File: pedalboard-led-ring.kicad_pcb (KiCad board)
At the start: 2 copper layers, 28 x 28 mm, 26 parts, among them J1 Conn_02x02_Odd_Even

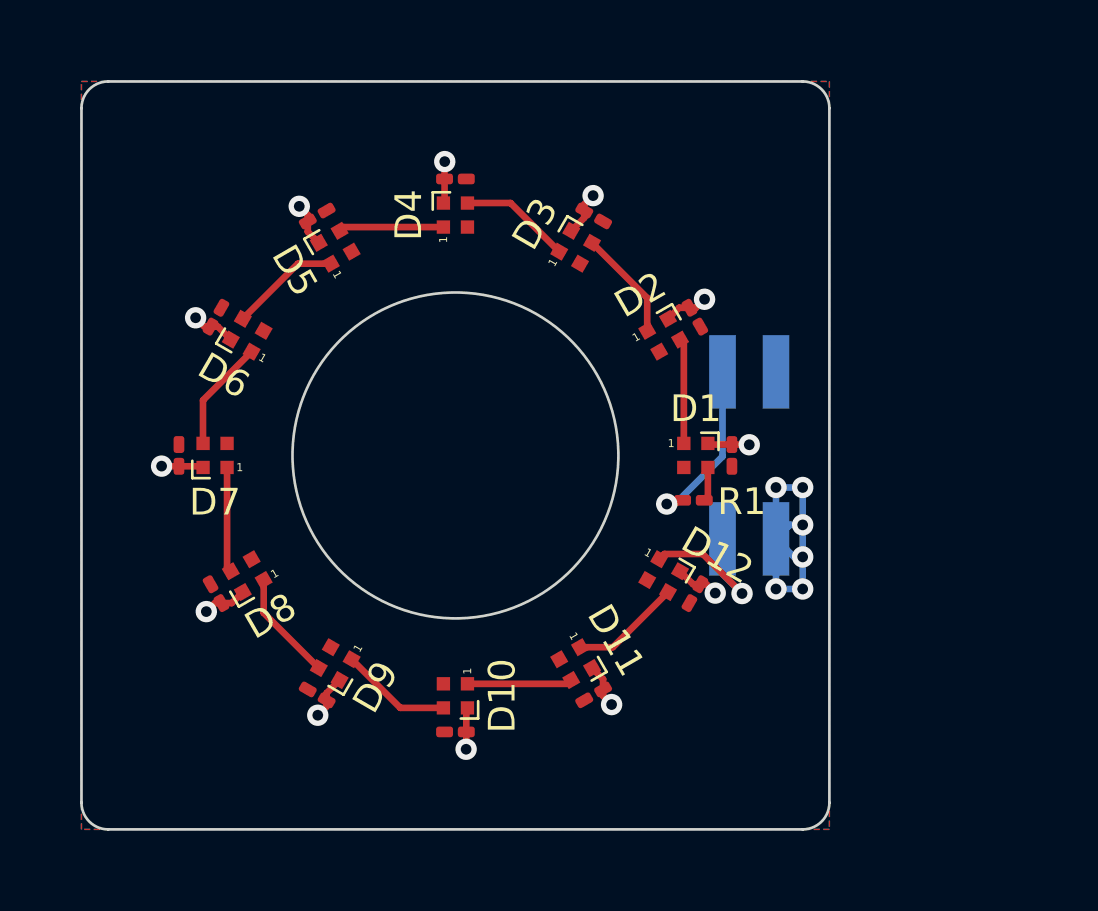
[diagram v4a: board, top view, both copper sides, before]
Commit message: Add 2nd connector port
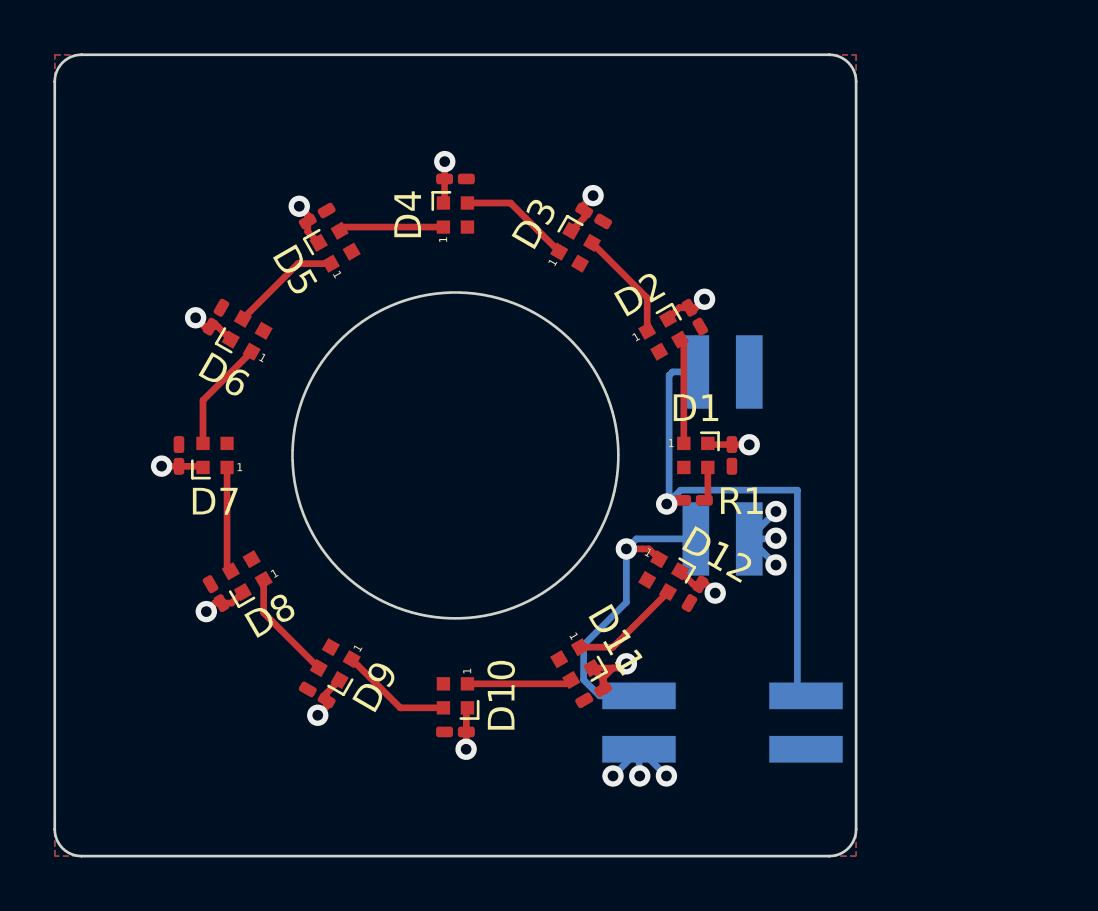
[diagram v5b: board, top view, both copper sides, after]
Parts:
- added J2: edge, Connector_PinSocket_2.00mm:PinSocket_2x02_P2.00mm_Vertical_SMD, B.Cu at (90.0, 70.0)
- J1: value Conn_02x02_Odd_Even -> middle
- moved J1 1.00 mm to (90.0, 60.0)
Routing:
- net Net-(J1-Pin_3): track 6.50 -> 19.4 mm
- net Net-(D12-DOUT): track 6.18 -> 12.0 mm
- net GND: track 12.1 -> 7.71 mm
- net VCC: track 19.3 -> 21.0 mm
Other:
- board size 28 x 28 mm -> 30 x 30 mm

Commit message: Move vias outside of keep out area
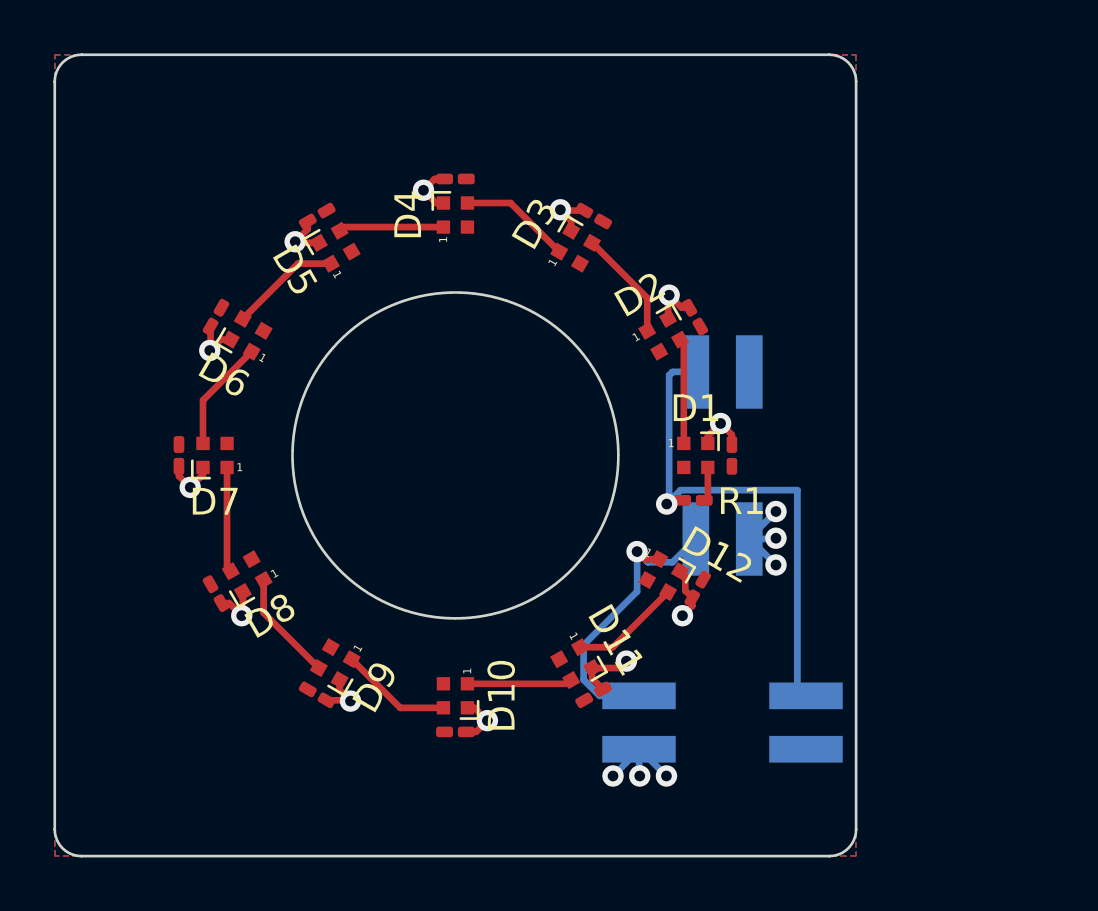
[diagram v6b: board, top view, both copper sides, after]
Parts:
- moved C12 0.20 mm to (89.1, 65.0), turned to 60 degrees
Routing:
- net VCC: track 21.0 -> 23.2 mm
- net Net-(J1-Pin_3): track 19.4 -> 18.8 mm

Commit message: Add 3 mounting holes
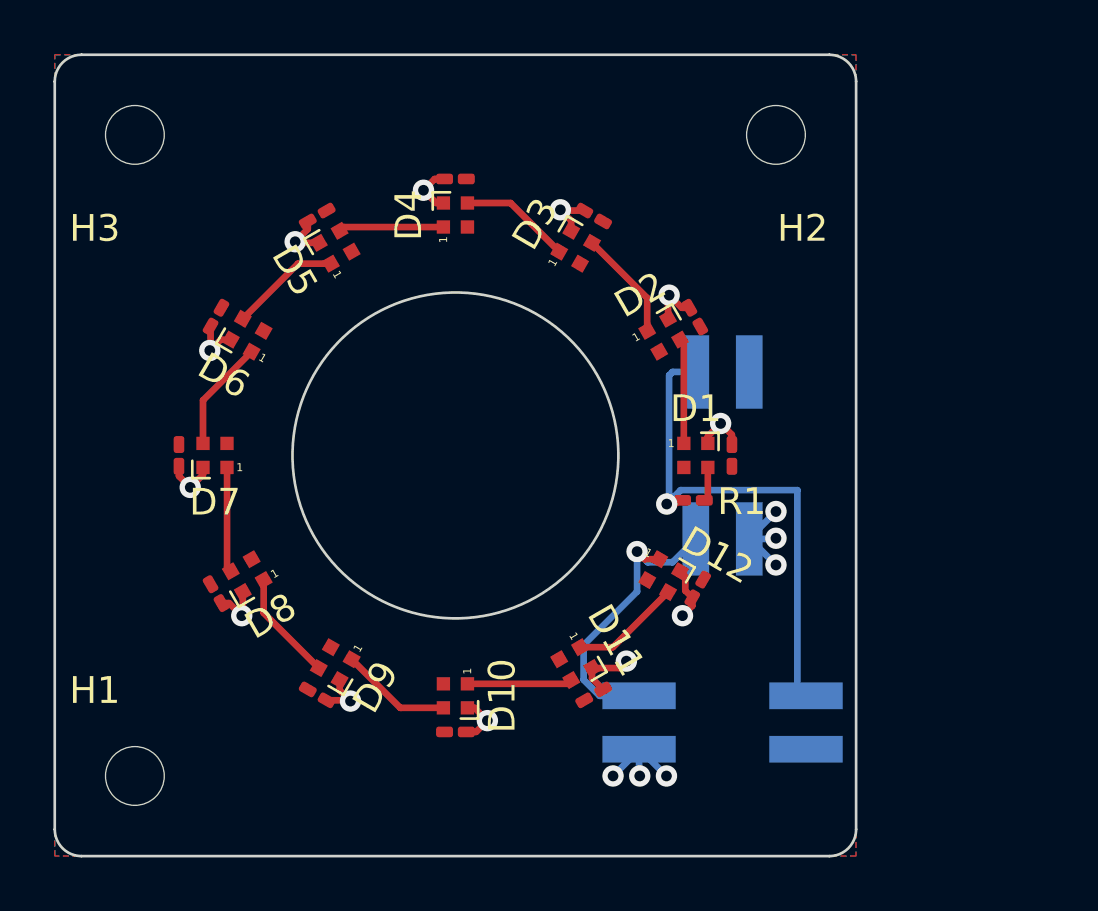
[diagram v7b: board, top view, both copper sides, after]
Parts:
- added H1: MountingHole, MountingHole:MountingHole_2.2mm_M2, F.Cu at (68.0, 72.0)
- added H2: MountingHole, MountingHole:MountingHole_2.2mm_M2, F.Cu at (92.0, 48.0)
- added H3: MountingHole, MountingHole:MountingHole_2.2mm_M2, F.Cu at (68.0, 48.0)
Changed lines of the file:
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@@
     )
+  )
+  (footprint "MountingHole:MountingHole_2.2mm_M2" (layer "F.Cu")
+    (at 68 48)
+    (descr "Mounting Hole 2.2mm, no annular, M2")
+    (tags "mounting hole 2.2mm no annular m2")
+    (property "Sheetfile" "pedalboard-led-ring.kicad_sch")
+    (property "Sheetname" "")
+    (property "ki_description" "Mounting Hole without connection")
+    (property "ki_keywords" "mounting hole")
+    (attr exclude_from_pos_files)
+    (fp_text reference "H3" (at -1.5 3.5) (layer "F.SilkS")
+        (effects (font (size 1 1) (thickness 0.15)))
+    )
+    (fp_text value "MountingHole" (at 0 3.2) (layer "F.Fab")
+        (effects (font (size 1 1) (thickness 0.15)))
+    )
+    (fp_text user "${REFERENCE}" (at 0 0) (layer "F.Fab")
+        (effects (font (size 1 1) (thickness 0.15)))
+    )
+    (fp_circle (center 0 0) (end 2.2 0)
+      (stroke (width 0.15) (type solid)) (fill none) (layer "Cmts.User"))
+    (fp_circle (center 0 0) (end 2.45 0)
+      (stroke (width 0.05) (type solid)) (fill none) (layer "F.CrtYd"))
+    (pad "" np_thru_hole circle (at 0 0) (size 2.2 2.2) (drill 2.2) (layers "*.Cu" "*.Mask"))
   )
   (footprint "LED_SMD:LED_SK6812_EC15_1.5x1.5mm" (layer "F.Cu")
@@
     )
   )
+  (footprint "MountingHole:MountingHole_2.2mm_M2" (layer "F.Cu")
+    (at 92 48)
+    (descr "Mounting Hole 2.2mm, no annular, M2")
+    (tags "mounting hole 2.2mm no annular m2")
+    (property "Sheetfile" "pedalboard-led-ring.kicad_sch")
+    (property "Sheetname" "")
+    (property "ki_description" "Mounting Hole without connection")
+    (property "ki_keywords" "mounting hole")
+    (attr exclude_from_pos_files)
+    (fp_text reference "H2" (at 1 3.5) (layer "F.SilkS")
+        (effects (font (size 1 1) (thickness 0.15)))
+    )
+    (fp_text value "MountingHole" (at 0 3.2) (layer "F.Fab")
+        (effects (font (size 1 1) (thickness 0.15)))
+    )
+    (fp_text user "${REFERENCE}" (at 0 0) (layer "F.Fab")
+        (effects (font (size 1 1) (thickness 0.15)))
+    )
+    (fp_circle (center 0 0) (end 2.2 0)
+      (stroke (width 0.15) (type solid)) (fill none) (layer "Cmts.User"))
+    (fp_circle (center 0 0) (end 2.45 0)
+      (stroke (width 0.05) (type solid)) (fill none) (layer "F.CrtYd"))
+    (pad "" np_thru_hole circle (at 0 0) (size 2.2 2.2) (drill 2.2) (layers "*.Cu" "*.Mask"))
+  )
   (footprint "Capacitor_SMD:C_0201_0603Metric_Pad0.64x0.40mm_HandSolder" (layer "F.Cu")
     (at 71.036637 54.825 60)
@@
     )
   )
+  (footprint "MountingHole:MountingHole_2.2mm_M2" (layer "F.Cu")
+    (at 68 72)
+    (descr "Mounting Hole 2.2mm, no annular, M2")
+    (tags "mounting hole 2.2mm no annular m2")
+    (property "Sheetfile" "pedalboard-led-ring.kicad_sch")
+    (property "Sheetname" "")
+    (property "ki_description" "Mounting Hole without connection")
+    (property "ki_keywords" "mounting hole")
+    (attr exclude_from_pos_files)
+    (fp_text reference "H1" (at -1.5 -3.2) (layer "F.SilkS")
+        (effects (font (size 1 1) (thickness 0.15)))
+    )
+    (fp_text value "MountingHole" (at 0 3.2) (layer "F.Fab")
+        (effects (font (size 1 1) (thickness 0.15)))
+    )
+    (fp_text user "${REFERENCE}" (at 0 0) (layer "F.Fab")
+        (effects (font (size 1 1) (thickness 0.15)))
+    )
+    (fp_circle (center 0 0) (end 2.2 0)
+      (stroke (width 0.15) (type solid)) (fill none) (layer "Cmts.User"))
+    (fp_circle (center 0 0) (end 2.45 0)
+      (stroke (width 0.05) (type solid)) (fill none) (layer "F.CrtYd"))
+    (pad "" np_thru_hole circle (at 0 0) (size 2.2 2.2) (drill 2.2) (layers "*.Cu" "*.Mask"))
+  )
   (footprint "LED_SMD:LED_SK6812_EC15_1.5x1.5mm" (layer "F.Cu")

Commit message: Silkscreen improvements
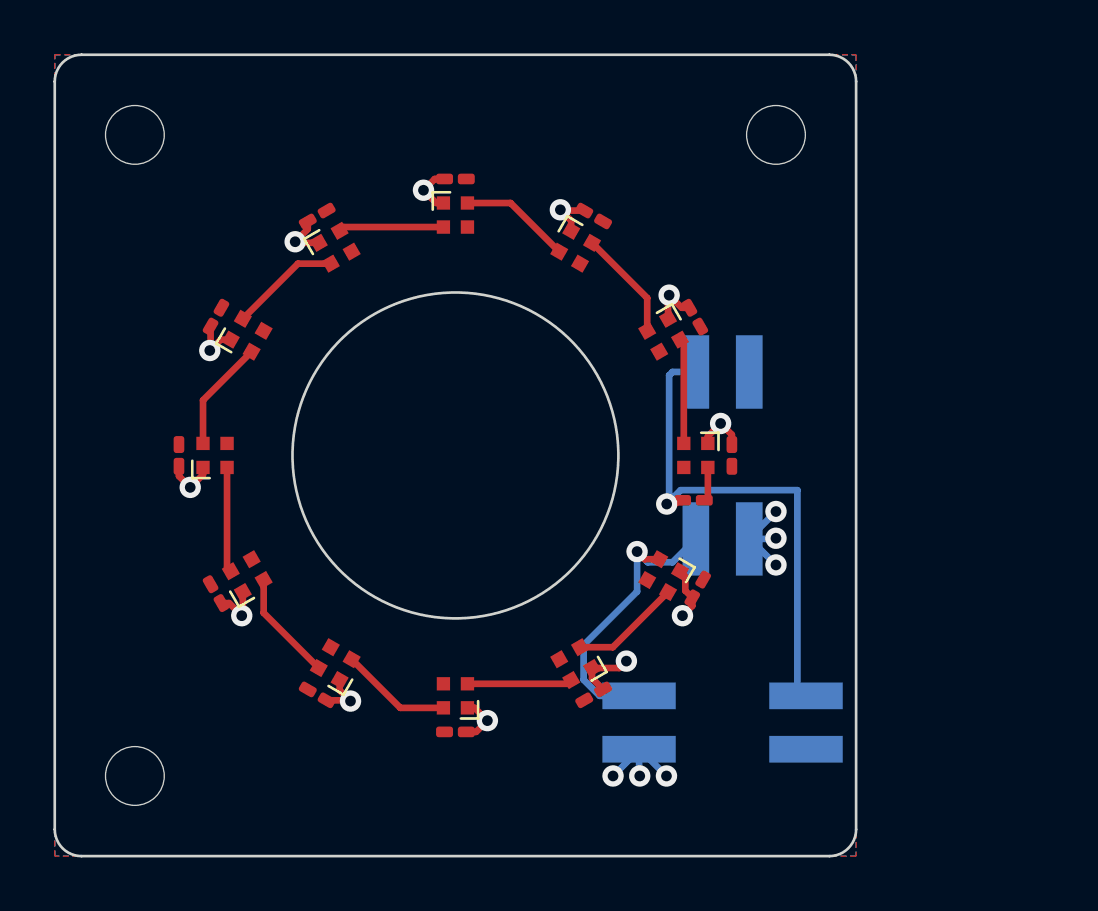
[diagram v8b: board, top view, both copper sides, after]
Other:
- board text added: "D0"
- board text added: "DI"
- board text added: "DO"
- board text added: "GND"
- board text added: "VCC"
